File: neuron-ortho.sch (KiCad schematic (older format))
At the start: 134 parts, among them J1 USB_C_Receptacle_USB2.0, J2 Conn_01x04_Male, J3 Conn_01x06_Male, Q1 DTC123J, SW1 SW_Push, U1 STM32F303C6Tx, U2 NCP1117-3.3_SOT223, U3 USBLC6-2SC6, Y1 8MHz

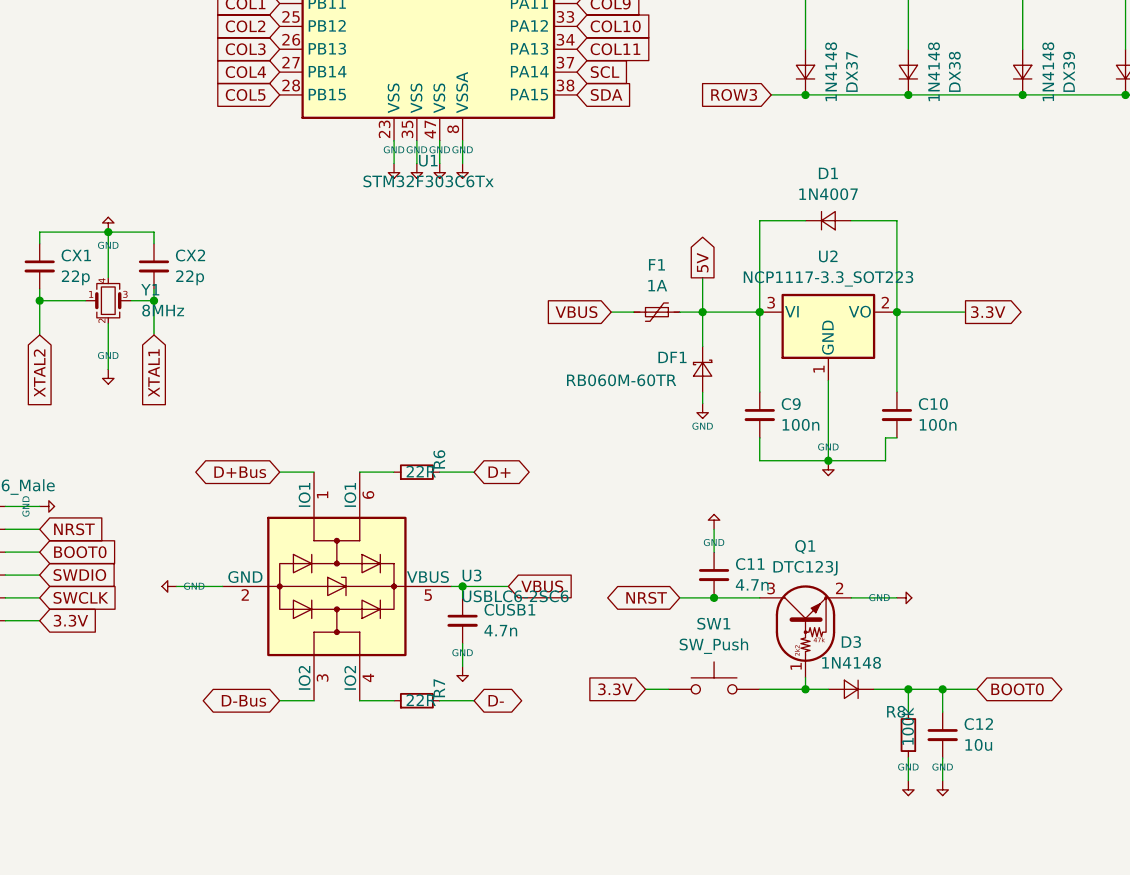
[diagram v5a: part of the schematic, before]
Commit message: Deleted traces, move component placing
Got some tips from Xelus and started over with component placement. New traces next
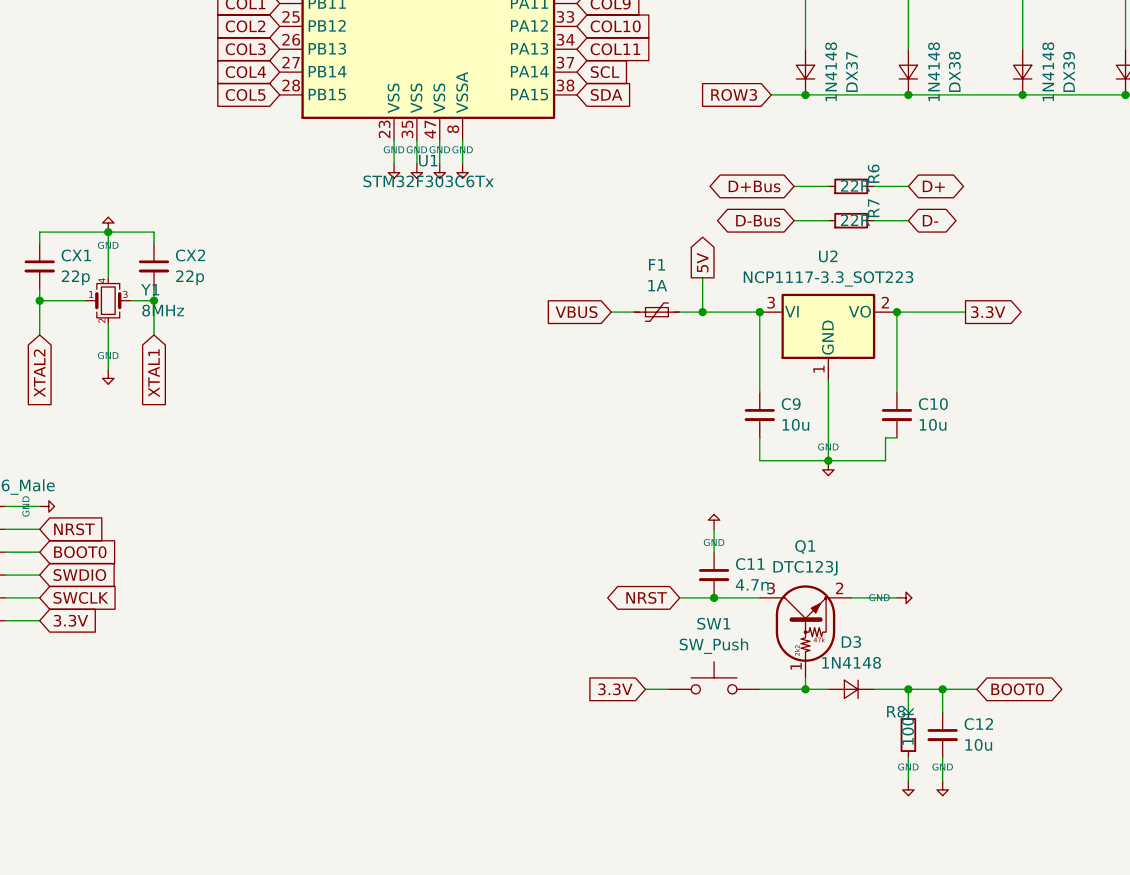
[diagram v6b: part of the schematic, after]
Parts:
- removed CUSB1: 4.7n, Capacitor_SMD:C_0805_2012Metric, symbol Device:C_Small
- removed D1: 1N4007, Diode_SMD:D_SOD-123, symbol Device:D_Small
- removed DF1: RB060M-60TR, Diode_SMD:D_SOD-123, symbol Device:D_Schottky_Small
- removed U3: USBLC6-2SC6, Package_TO_SOT_SMD:SOT-23-6, symbol Power_Protection:USBLC6-2SC6
- C10, C9: value 100n -> 10u
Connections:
- net D+Bus: now also R6.1
- net D-Bus: now also R7.1
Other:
- moved on the sheet: R6, R7
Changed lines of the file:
@@
 	1    0    0    -1
-$EndComp
-Wire Wire Line
-	3500 7050 3350 7050
-Wire Wire Line
-	4050 7050 4200 7050
-Wire Wire Line
-	3700 7050 3850 7050
-Wire Wire Line
-	4100 6550 4150 6550
-Wire Wire Line
-	3500 6050 3350 6050
-Wire Wire Line
-	2900 6550 3100 6550
-Text GLabel 4200 7050 2    50   BiDi ~ 0
-D-
-$Comp
-L Device:R_Small R7
-U 1 1 5E777318
-P 3950 7050
-F 0 "R7" H 4050 6950 50  0000 R CNN
-F 1 "22R" V 3950 7100 50  0000 R CNN
-F 2 "Resistor_SMD:R_0805_2012Metric" H 3950 7050 50  0001 C CNN
-F 3 "~" H 3950 7050 50  0001 C CNN
-	1    3950 7050
-	0    -1   -1   0
-$EndComp
-Text GLabel 3350 6050 0    50   BiDi ~ 0
-D+Bus
-Text GLabel 3350 7050 0    50   BiDi ~ 0
-D-Bus
-Text GLabel 4350 6550 2    50   Input ~ 0
-VBUS
-$Comp
-L keyboard_parts:GND #PWR020
-U 1 1 5E772B04
-P 2900 6550
-F 0 "#PWR020" H 2900 6600 20  0001 C CNN
-F 1 "GND" V 2900 6579 30  0000 L CNN
-F 2 "" H 2900 6550 60  0000 C CNN
-F 3 "" H 2900 6550 60  0000 C CNN
-	1    2900 6550
-	0    1    1    0
 $EndComp
 $Comp
@@
 P 5450 5800
 F 0 "C9" H 5542 5846 50  0000 L CNN
-F 1 "100n" H 5542 5755 50  0000 L CNN
+F 1 "10u" H 5542 5755 50  0000 L CNN
 F 2 "Capacitor_SMD:C_0805_2012Metric" H 5450 5800 50  0001 C CNN
 F 3 "~" H 5450 5800 50  0001 C CNN
@@
 P 6050 5800
 F 0 "C10" H 6142 5846 50  0000 L CNN
-F 1 "100n" H 6142 5755 50  0000 L CNN
+F 1 "10u" H 6142 5755 50  0000 L CNN
 F 2 "Capacitor_SMD:C_0805_2012Metric" H 6050 5800 50  0001 C CNN
 F 3 "~" H 6050 5800 50  0001 C CNN
 	1    6050 5800
-	1    0    0    -1
-$EndComp
-$Comp
-L keyboard_parts:GND #PWR017
-U 1 1 5E7B3157
-P 5200 5750
-F 0 "#PWR017" H 5200 5800 20  0001 C CNN
-F 1 "GND" H 5200 5650 30  0000 C CNN
-F 2 "" H 5200 5750 60  0000 C CNN
-F 3 "" H 5200 5750 60  0000 C CNN
-	1    5200 5750
-	1    0    0    -1
-$EndComp
-$Comp
-L Device:D_Small D1
-U 1 1 5E7B385C
-P 5750 4950
-F 0 "D1" H 5750 5155 50  0000 C CNN
-F 1 "1N4007" H 5750 5064 50  0000 C CNN
-F 2 "Diode_SMD:D_SOD-123" V 5750 4950 50  0001 C CNN
-F 3 "~" V 5750 4950 50  0001 C CNN
-	1    5750 4950
 	1    0    0    -1
 $EndComp
@@
 Wire Wire Line
 	5100 5350 5200 5350
-Wire Wire Line
-	5200 5350 5200 5500
 Connection ~ 5200 5350
 Wire Wire Line
@@
 Wire Wire Line
 	6050 5700 6050 5350
-Wire Wire Line
-	6050 5350 6050 4950
-Wire Wire Line
-	6050 4950 5850 4950
 Connection ~ 6050 5350
-Wire Wire Line
-	5650 4950 5450 4950
-Wire Wire Line
-	5450 4950 5450 5350
 Text GLabel 6350 5350 2    50   Output ~ 0
 3.3V
@@
 	1    0    0    -1
 $EndComp
-Text GLabel 4950 7000 0    50   Input ~ 0
-3.3V
 Text GLabel 6400 7000 2    50   BiDi ~ 0
 BOOT0
@@
 Wire Wire Line
 	5050 7000 4950 7000
-Wire Wire Line
-	5200 5700 5200 5750
-$Comp
-L Device:D_Schottky_Small DF1
-U 1 1 5E6F97CE
-P 5200 5600
-F 0 "DF1" V 5150 5400 50  0000 L CNN
-F 1 "RB060M-60TR" V 5250 5000 50  0000 L CNN
-F 2 "Diode_SMD:D_SOD-123" V 5200 5600 50  0001 C CNN
-F 3 "~" V 5200 5600 50  0001 C CNN
-	1    5200 5600
-	0    1    1    0
-$EndComp
-$Comp
-L Device:C_Small CUSB1
-U 1 1 5E7015F0
-P 4150 6700
-F 0 "CUSB1" H 4242 6746 50  0000 L CNN
-F 1 "4.7n" H 4242 6655 50  0000 L CNN
-F 2 "Capacitor_SMD:C_0805_2012Metric" H 4150 6700 50  0001 C CNN
-F 3 "~" H 4150 6700 50  0001 C CNN
-	1    4150 6700
-	1    0    0    -1
-$EndComp
-$Comp
-L keyboard_parts:GND #PWR022
-U 1 1 5E701F7F
-P 4150 6900
-F 0 "#PWR022" H 4150 6950 20  0001 C CNN
-F 1 "GND" H 4150 6959 30  0000 C CNN
-F 2 "" H 4150 6900 60  0000 C CNN
-F 3 "" H 4150 6900 60  0000 C CNN
-	1    4150 6900
-	1    0    0    -1
-$EndComp
-Wire Wire Line
-	4150 6600 4150 6550
-Connection ~ 4150 6550
-Wire Wire Line
-	4150 6550 4350 6550
-Wire Wire Line
-	4150 6800 4150 6900
 $Comp
 L Device:Crystal_GND24_Small Y1
@@
 F 3 "" H 5625 2525 60  0001 C CNN
 	1    6250 2550
-	1    0    0    -1
-$EndComp
-$Comp
-L MX_Alps_Hybrid:MX-NoLED MX25
-U 1 1 5E753E5D
-P 5800 2550
-F 0 "MX25" H 5833 2773 60  0000 C CNN
-F 1 "MX-NoLED" H 5833 2699 20  0000 C CNN
-F 2 "MX_Alps_Hybrid:MX-1U-NoLED" H 5175 2525 60  0001 C CNN
-F 3 "" H 5175 2525 60  0001 C CNN
-	1    5800 2550
 	1    0    0    -1
 $EndComp
@@
 Text GLabel 2300 6300 2    50   Input ~ 0
 NRST
-Text GLabel 2300 6400 2    50   Input ~ 0
-BOOT0
-Text GLabel 2300 6500 2    50   Input ~ 0
-SWDIO
-Text GLabel 2300 6600 2    50   Input ~ 0
-SWCLK
 Text GLabel 2300 6700 2    50   Input ~ 0
 3.3V
@@
 Wire Wire Line
 	6100 3750 6100 4200
-$Comp
-L Power_Protection:USBLC6-2SC6 U3
-U 1 1 5E771176
-P 3600 6550
-F 0 "U3" V 3554 7094 50  0000 L CNN
-F 1 "USBLC6-2SC6" V 3645 7094 50  0000 L CNN
-F 2 "Package_TO_SOT_SMD:SOT-23-6" H 2850 6950 50  0001 C CNN
-F 3 "http://www2.st.com/resource/en/datasheet/CD00050750.pdf" H 3800 6900 50  0001 C CNN
-	1    3600 6550
-	0    1    1    0
-$EndComp
-Wire Wire Line
-	3700 6050 3850 6050
-$Comp
-L Device:R_Small R6
-U 1 1 5E774FC3
-P 3950 6050
-F 0 "R6" H 4050 5950 50  0000 R CNN
-F 1 "22R" V 3950 6100 50  0000 R CNN
-F 2 "Resistor_SMD:R_0805_2012Metric" H 3950 6050 50  0001 C CNN
-F 3 "~" H 3950 6050 50  0001 C CNN
-	1    3950 6050
-	0    -1   -1   0
-$EndComp
-Wire Wire Line
-	4200 6050 4050 6050
-Text GLabel 4200 6050 2    50   BiDi ~ 0
-D+
 NoConn ~ 3350 3900
 NoConn ~ 3350 3200
@@
 Text GLabel 4650 4400 2    50   Input ~ 0
 SDA
+Text GLabel 6100 4800 2    50   BiDi ~ 0
+D+
+Wire Wire Line
+	6100 4800 5950 4800
+$Comp
+L Device:R_Small R6
+U 1 1 5E774FC3
+P 5850 4800
+F 0 "R6" H 5950 4700 50  0000 R CNN
+F 1 "22R" V 5850 4850 50  0000 R CNN
+F 2 "Resistor_SMD:R_0805_2012Metric" H 5850 4800 50  0001 C CNN
+F 3 "~" H 5850 4800 50  0001 C CNN
+	1    5850 4800
+	0    -1   -1   0
+$EndComp
+Text GLabel 2300 6600 2    50   Input ~ 0
+SWCLK
+Text GLabel 2300 6500 2    50   Input ~ 0
+SWDIO
+Text GLabel 2300 6400 2    50   Input ~ 0
+BOOT0
+Text GLabel 4950 7000 0    50   Input ~ 0
+3.3V
+Text GLabel 5600 4950 0    50   BiDi ~ 0
+D-Bus
+Text GLabel 5600 4800 0    50   BiDi ~ 0
+D+Bus
+$Comp
+L Device:R_Small R7
+U 1 1 5E777318
+P 5850 4950
+F 0 "R7" H 5950 4850 50  0000 R CNN
+F 1 "22R" V 5850 5000 50  0000 R CNN
+F 2 "Resistor_SMD:R_0805_2012Metric" H 5850 4950 50  0001 C CNN
+F 3 "~" H 5850 4950 50  0001 C CNN
+	1    5850 4950
+	0    -1   -1   0
+$EndComp
+Text GLabel 6100 4950 2    50   BiDi ~ 0
+D-
+Wire Wire Line
+	5950 4950 6100 4950
+Wire Wire Line
+	5600 4800 5750 4800
+Wire Wire Line
+	5600 4950 5750 4950
+$Comp
+L MX_Alps_Hybrid:MX-NoLED MX25
+U 1 1 5E753E5D
+P 5800 2550
+F 0 "MX25" H 5833 2773 60  0000 C CNN
+F 1 "MX-NoLED" H 5833 2699 20  0000 C CNN
+F 2 "MX_Alps_Hybrid:MX-1U-NoLED" H 5175 2525 60  0001 C CNN
+F 3 "" H 5175 2525 60  0001 C CNN
+	1    5800 2550
+	1    0    0    -1
+$EndComp
 $EndSCHEMATC

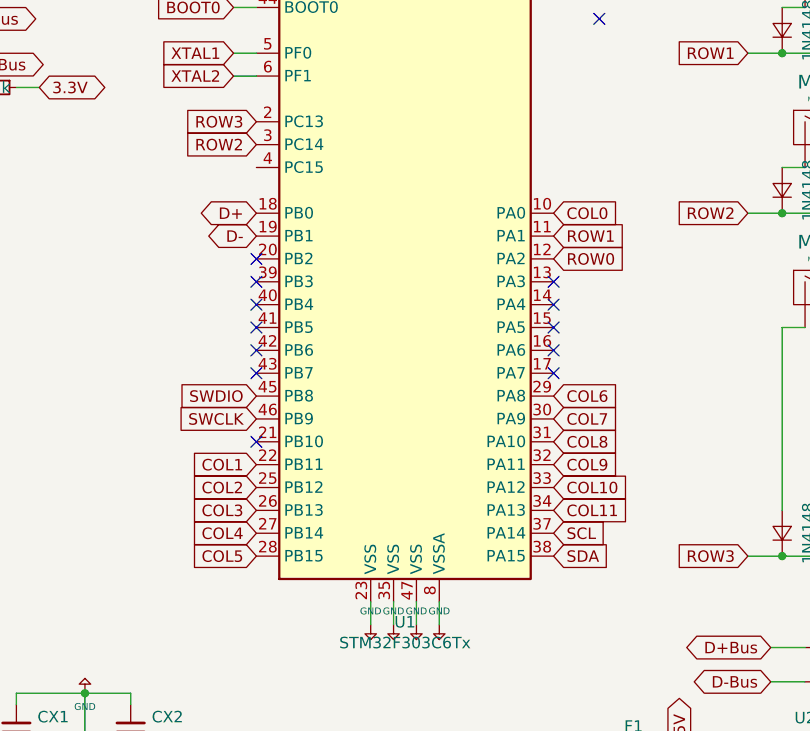
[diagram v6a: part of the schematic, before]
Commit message: Finished non-switch matrix traces
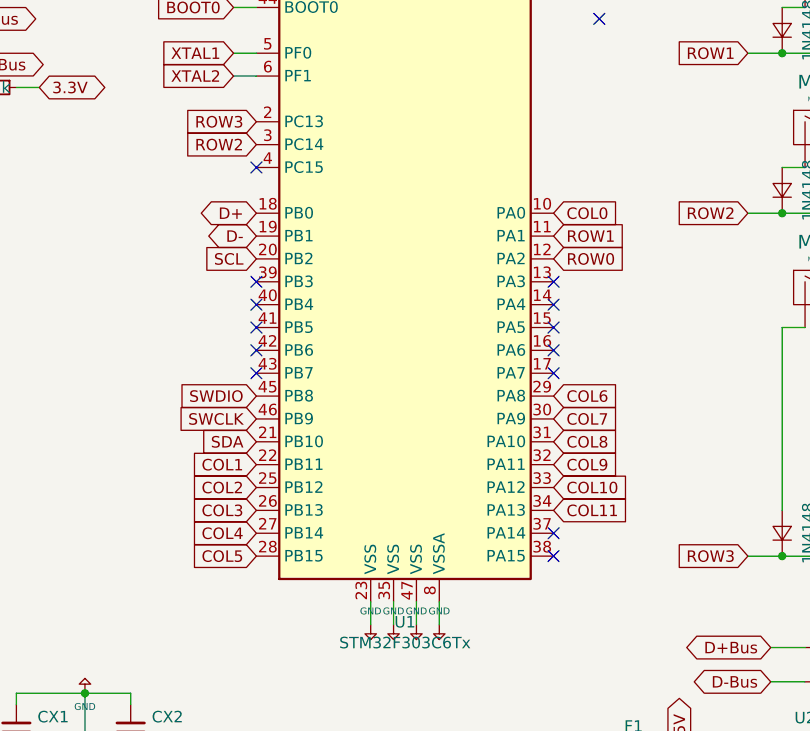
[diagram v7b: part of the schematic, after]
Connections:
- net SCL: now also U1.20 (PB2); no longer U1.37 (PA14)
- net SDA: now also U1.21 (PB10); no longer U1.38 (PA15)
- no-connect marks 17 -> 18
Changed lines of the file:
@@
-$EndComp
-$Comp
-L MCU_ST_STM32F3:STM32F303C6Tx U1
-U 1 1 5E6E2385
-P 4050 3100
-F 0 "U1" H 4000 1511 50  0000 C CNN
-F 1 "STM32F303C6Tx" H 4000 1420 50  0000 C CNN
-F 2 "Package_QFP:LQFP-48_7x7mm_P0.5mm" H 3450 1700 50  0001 R CNN
-F 3 "http://www.st.com/st-web-ui/static/active/en/resource/technical/document/datasheet/DM00092070.pdf" H 4050 3100 50  0001 C CNN
-	1    4050 3100
-	1    0    0    -1
 $EndComp
 $Comp
@@
 Text GLabel 3350 3800 0    50   Input ~ 0
 SWCLK
-Text GLabel 4650 4300 2    50   Input ~ 0
+Text GLabel 3350 3100 0    50   Input ~ 0
 SCL
 Text GLabel 4050 1200 3    50   BiDi ~ 0
 3.3V
-Wire Wire Line
-	4250 1600 4150 1600
-Connection ~ 3850 1600
-Wire Wire Line
-	3850 1600 3750 1600
-Connection ~ 3950 1600
-Wire Wire Line
-	3950 1600 3850 1600
-Connection ~ 4050 1600
-Wire Wire Line
-	4050 1600 3950 1600
-Connection ~ 4150 1600
-Wire Wire Line
-	4150 1600 4050 1600
 Wire Wire Line
 	4050 1200 4050 1050
@@
 Wire Wire Line
 	6100 3750 6100 4200
-NoConn ~ 3350 3900
 NoConn ~ 3350 3200
-NoConn ~ 3350 3100
 NoConn ~ 4650 3200
 NoConn ~ 4850 2050
@@
 NoConn ~ 4650 3500
 NoConn ~ 4650 3600
-Text GLabel 4650 4400 2    50   Input ~ 0
+Text GLabel 3350 3900 0    50   Input ~ 0
 SDA
 Text GLabel 6100 4800 2    50   BiDi ~ 0
@@
 	1    0    0    -1
 $EndComp
+Wire Wire Line
+	4250 1600 4150 1600
+Connection ~ 4150 1600
+Wire Wire Line
+	4150 1600 4050 1600
+Connection ~ 4050 1600
+Wire Wire Line
+	4050 1600 3950 1600
+Connection ~ 3950 1600
+Wire Wire Line
+	3950 1600 3850 1600
+Wire Wire Line
+	3850 1600 3750 1600
+Connection ~ 3850 1600
+$Comp
+L MCU_ST_STM32F3:STM32F303C6Tx U1
+U 1 1 5E6E2385
+P 4050 3100
+F 0 "U1" H 4000 1511 50  0000 C CNN
+F 1 "STM32F303C6Tx" H 4000 1420 50  0000 C CNN
+F 2 "Package_QFP:LQFP-48_7x7mm_P0.5mm" H 3450 1700 50  0001 R CNN
+F 3 "http://www.st.com/st-web-ui/static/active/en/resource/technical/document/datasheet/DM00092070.pdf" H 4050 3100 50  0001 C CNN
+	1    4050 3100
+	1    0    0    -1
+$EndComp
+NoConn ~ 3350 2700
+NoConn ~ 4650 4400
+NoConn ~ 4650 4300
 $EndSCHEMATC

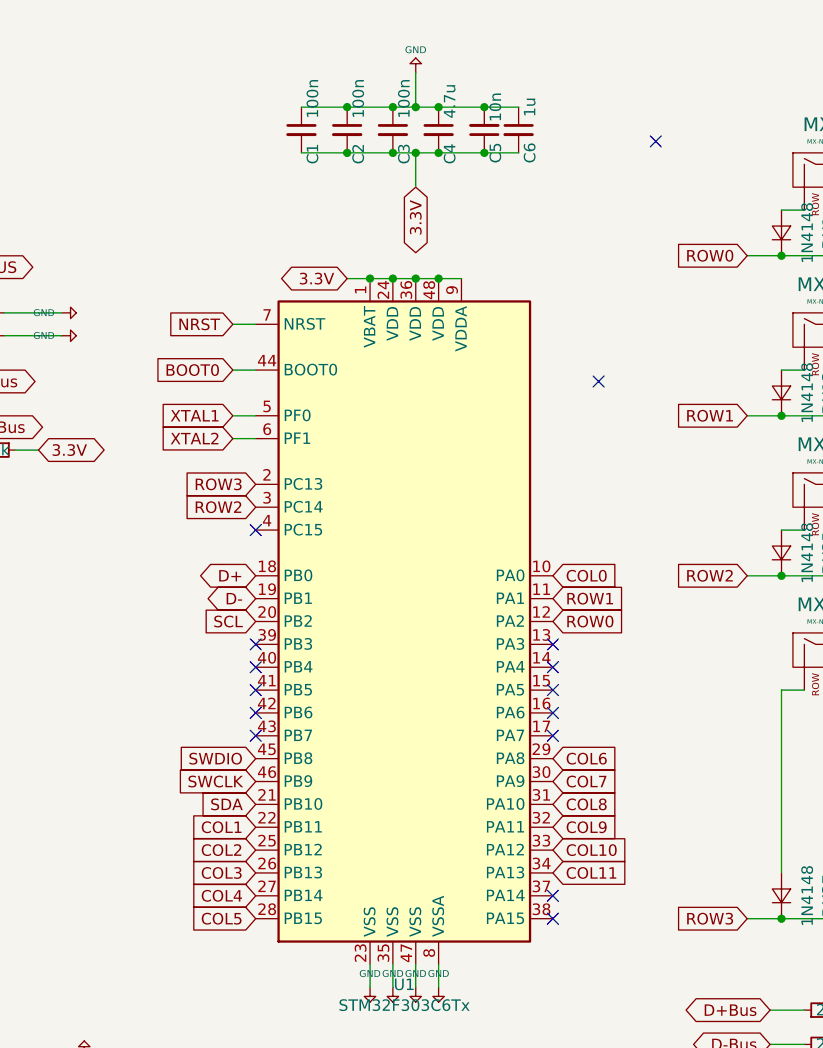
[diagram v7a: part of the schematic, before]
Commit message: Switch matrix traces done
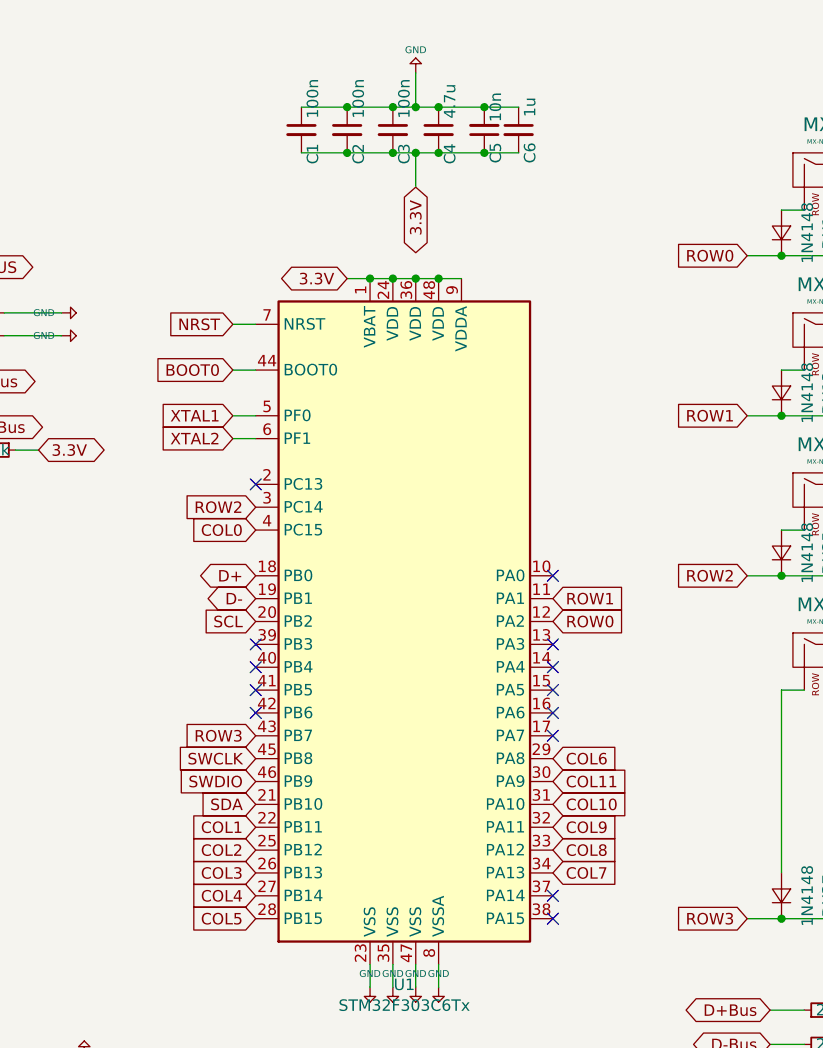
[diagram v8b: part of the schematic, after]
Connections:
- net COL0: now also U1.4 (PC15); no longer U1.10 (PA0)
- net COL10: now also U1.31 (PA10); no longer U1.33 (PA12)
- net COL11: now also U1.30 (PA9); no longer U1.34 (PA13)
- net COL7: now also U1.34 (PA13); no longer U1.30 (PA9)
- net COL8: now also U1.33 (PA12); no longer U1.31 (PA10)
- net ROW3: now also U1.43 (PB7); no longer U1.2 (PC13)
- net SWCLK: now also U1.45 (PB8); no longer U1.46 (PB9)
- net SWDIO: now also U1.46 (PB9); no longer U1.45 (PB8)
- no-connect marks 18 -> 16
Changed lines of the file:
@@
 Text GLabel 3350 2900 0    50   BiDi ~ 0
 D+
-Text GLabel 4650 2900 2    50   Input ~ 0
+Text GLabel 3350 2700 0    50   Input ~ 0
 COL0
 Text GLabel 3350 4000 0    50   Input ~ 0
@@
 Text GLabel 3350 2600 0    50   Input ~ 0
 ROW2
-Text GLabel 3350 2500 0    50   Input ~ 0
+Text GLabel 3350 3600 0    50   Input ~ 0
 ROW3
 Text GLabel 3350 4200 0    50   Input ~ 0
@@
 Text GLabel 4650 3700 2    50   Input ~ 0
 COL6
-Text GLabel 4650 3800 2    50   Input ~ 0
+Text GLabel 4650 4200 2    50   Input ~ 0
 COL7
-Text GLabel 4650 3900 2    50   Input ~ 0
+Text GLabel 4650 4100 2    50   Input ~ 0
 COL8
 Text GLabel 4650 4000 2    50   Input ~ 0
 COL9
-Text GLabel 4650 4100 2    50   Input ~ 0
+Text GLabel 4650 3900 2    50   Input ~ 0
 COL10
-Text GLabel 4650 4200 2    50   Input ~ 0
+Text GLabel 4650 3800 2    50   Input ~ 0
 COL11
 $Comp
@@
 Text GLabel 3250 2000 0    50   Input ~ 0
 BOOT0
+Text GLabel 3350 3800 0    50   Input ~ 0
+SWDIO
 Text GLabel 3350 3700 0    50   Input ~ 0
-SWDIO
-Text GLabel 3350 3800 0    50   Input ~ 0
 SWCLK
 Text GLabel 3350 3100 0    50   Input ~ 0
@@
 NoConn ~ 3350 3200
 NoConn ~ 4650 3200
-NoConn ~ 4850 2050
-NoConn ~ 5100 1000
 NoConn ~ 2100 8550
 NoConn ~ 3350 3300
 NoConn ~ 3350 3400
 NoConn ~ 3350 3500
-NoConn ~ 3350 3600
 NoConn ~ 4650 3300
 NoConn ~ 4650 3400
 NoConn ~ 4650 3500
 NoConn ~ 4650 3600
-Text GLabel 3350 3900 0    50   Input ~ 0
-SDA
 Text GLabel 6100 4800 2    50   BiDi ~ 0
 D+
@@
 	1    0    0    -1
 $EndComp
-NoConn ~ 3350 2700
+Text GLabel 3350 3900 0    50   Input ~ 0
+SDA
 NoConn ~ 4650 4400
 NoConn ~ 4650 4300
+NoConn ~ 4650 2900
+NoConn ~ 3350 2500
 $EndSCHEMATC
